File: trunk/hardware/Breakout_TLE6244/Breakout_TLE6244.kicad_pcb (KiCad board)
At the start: 2 copper layers, 1 part

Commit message: draft #1
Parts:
- removed Test: VAL**, HiQUAD64
- added C1001: 1uF, SM0805, B.Cu at (233.0, 147.3)
- added C1002: .01uF, SM0805, B.Cu at (234.9, 147.3)
- added D1001: LED-red, LED-0805_A, F.Cu at (207.6, 122.6)
- added D1002: LED-red, LED-0805_A, F.Cu at (207.6, 128.9)
- added D1003: LED-red, LED-0805_A, F.Cu at (207.6, 134.0)
- added D1004: LED-red, LED-0805_A, F.Cu at (207.6, 139.1)
- added D1005: LED-red, LED-0805_A, F.Cu at (207.6, 144.1)
- added D1006: LED-red, LED-0805_A, F.Cu at (207.6, 149.2)
- added D1007: LED-red, LED-0805_A, F.Cu at (207.6, 154.3)
- added D1008: LED-red, LED-0805_A, F.Cu at (207.6, 159.4)
- added D1009: DIODE, SOD-123, F.Cu at (203.8, 122.6)
- added D1010: DIODE, SOD-123, F.Cu at (203.8, 128.9)
- added D1011: DIODE, SOD-123, F.Cu at (203.2, 134.0)
- added D1012: DIODE, SOD-123, F.Cu at (203.2, 139.1)
- added D1013: DIODE, SOD-123, F.Cu at (203.2, 144.1)
- added D1014: DIODE, SOD-123, F.Cu at (203.2, 149.2)
- added D1015: DIODE, SOD-123, F.Cu at (203.2, 154.3)
- added D1016: DIODE, SOD-123, F.Cu at (203.2, 159.4)
- added D1017: DIODE, SOD-123, F.Cu at (215.9, 166.4)
- added D1018: LED-red, LED-0805_A, F.Cu at (211.5, 166.4)
- added D1019: DIODE, SOD-123, F.Cu at (236.2, 166.4)
- added D1020: LED-red, LED-0805_A, F.Cu at (240.7, 166.4)
- added D1021: DIODE, SOD-123, F.Cu at (249.6, 122.6)
- added D1022: DIODE, SOD-123, F.Cu at (249.6, 128.9)
- added D1023: DIODE, SOD-123, F.Cu at (249.6, 134.0)
- added D1024: DIODE, SOD-123, F.Cu at (249.6, 139.1)
- added D1025: DIODE, SOD-123, F.Cu at (249.6, 144.1)
- added D1026: DIODE, SOD-123, F.Cu at (249.6, 149.2)
- added D1027: DIODE, SOD-123, F.Cu at (249.6, 154.3)
- added D1028: DIODE, SOD-123, F.Cu at (249.6, 159.4)
- added D1029: LED-red, LED-0805_A, F.Cu at (245.1, 122.6)
- added D1030: LED-red, LED-0805_A, F.Cu at (245.1, 128.9)
- added D1031: LED-red, LED-0805_A, F.Cu at (245.1, 134.0)
- added D1032: LED-red, LED-0805_A, F.Cu at (245.1, 139.1)
- added D1033: LED-red, LED-0805_A, F.Cu at (245.1, 144.1)
- added D1034: LED-red, LED-0805_A, F.Cu at (245.1, 149.2)
- added D1035: LED-red, LED-0805_A, F.Cu at (245.1, 154.3)
- added D1036: LED-red, LED-0805_A, F.Cu at (245.1, 159.4)
- added K1001: CONN_3, bornier3, F.Cu at (196.8, 125.1)
- added K1002: CONN_3, bornier3, F.Cu at (196.8, 140.3)
- added K1003: CONN_3, bornier3, F.Cu at (196.8, 155.6)
- added K1004: CONN_3, bornier3, F.Cu at (226.1, 168.3)
- added K1005: CONN_3, bornier3, F.Cu at (255.9, 125.1)
- added K1006: CONN_3, bornier3, F.Cu at (255.9, 140.3)
- added K1007: CONN_3, bornier3, F.Cu at (255.9, 155.6)
- added P1001: CONN_10, SIL-10, F.Cu at (205.7, 170.8)
- added P1002: CONN_10, SIL-10, F.Cu at (246.4, 170.8)
- added P1003: CONN_8, SIL-8, F.Cu at (226.1, 127.6)
- added R1001: 1K, SM0805, F.Cu at (211.5, 122.6)
- added R1002: 1K, SM0805, F.Cu at (211.5, 128.9)
- added R1003: 1K, SM0805, F.Cu at (211.5, 134.0)
- added R1004: 1K, SM0805, F.Cu at (211.5, 139.1)
- added R1005: 1K, SM0805, F.Cu at (211.5, 144.1)
- added R1006: 1K, SM0805, F.Cu at (211.5, 149.2)
- added R1007: 1K, SM0805, F.Cu at (211.5, 154.3)
- added R1008: 1K, SM0805, F.Cu at (211.5, 159.4)
- added R1009: 1K, SM0805, F.Cu at (207.6, 166.4)
- added R1010: 1K, SM0805, F.Cu at (244.5, 166.4)
- added R1011: 1K, SM0805, F.Cu at (241.3, 122.6)
- added R1012: 1K, SM0805, F.Cu at (241.3, 128.9)
- added R1013: 1K, SM0805, F.Cu at (241.3, 134.0)
- added R1014: 1K, SM0805, F.Cu at (241.3, 139.1)
- added R1015: 1K, SM0805, F.Cu at (241.3, 144.1)
- added R1016: 1K, SM0805, F.Cu at (241.3, 149.2)
- added R1017: 1K, SM0805, F.Cu at (241.3, 154.3)
- added R1018: 1K, SM0805, F.Cu at (241.3, 159.4)
- added U1001: TLE6244, HiQUAD64, F.Cu at (226.1, 148.6)
- added W1001: TEST, SM0805_jumper, F.Cu at (229.2, 160.7)
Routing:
- added copper zone on PWR, net /DD_HIP9011/5V
- added copper zone on B.Cu, net GND
- added copper zone on F.Cu, net GND
- added copper zone on GND, net GND
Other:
- copper layers 2 -> 4
- net class 1A external added: clearance 0.2159, trace_width 0.3048, via_dia 0.6858, via_drill 0.3302
- net class 2.5A external added: clearance 0.2159, trace_width 1.0668, via_dia 0.6858, via_drill 0.3302
- net class 3.5A external added: clearance 0.2159, trace_width 1.651, via_dia 1.0922, via_drill 0.6858
- net class 5A external added: clearance 0.2159, trace_width 2.7178, via_dia 1.54178, via_drill 1.18618
- net class Default: clearance 0.254 -> 0.1524; trace_width 0.254 -> 0.1524; via_dia 0.889 -> 0.6858; via_drill 0.635 -> 0.3302
- net class min2_extern_.188A added: clearance 0.1524, trace_width 0.1524, via_dia 0.6858, via_drill 0.3302
- net class min_extern_.241A added: clearance 0.2159, trace_width 0.2159, via_dia 0.6858, via_drill 0.3302
- rule pad_to_mask_clearance: 0 -> 0.2
- rule trace_clearance: 0.254 -> 0.1524
- rule trace_min: 0.254 -> 0.1524
- rule via_min_drill: 0.508 -> 0.3302
- rule via_min_size: 0.889 -> 0

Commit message: fresh
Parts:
- removed C1001: 1uF, SM0805
- removed C1002: .01uF, SM0805
- removed D1017: DIODE, SOD-123
- removed D1020: LED-red, LED-0805_A
- removed P1001, P1002: CONN_10, SIL-10
- removed P1003: CONN_8, SIL-8
- added C1: 1uF, SM0805, B.Cu at (233.0, 147.3)
- added C2: .01uF, SM0805, B.Cu at (234.9, 147.3)
- added D17: DIODE, SOD-123, F.Cu at (215.9, 161.4)
- added D20: LED-red, LED-0805_A, F.Cu at (236.1, 166.2)
- added P1: CONN_4, SIL-4, F.Cu at (214.8, 138.4)
- added P2: CONN_3, SIL-3, F.Cu at (212.2, 146.0)
- added P3: CONN_2, SIL-2, F.Cu at (213.5, 148.7)
- added P4: CONN_3, SIL-3, F.Cu at (211.5, 163.8)
- added P5: CONN_5, SIL-5, F.Cu at (225.3, 133.0)
- added P6: CONN_3, SIL-3, F.Cu at (240.9, 163.8)
- added P7: CONN_2, SIL-2, F.Cu at (238.9, 145.9)
- added P8: CONN_2, SIL-2, F.Cu at (238.9, 148.7)
- moved D21 20.4 mm to (234.1, 135.9), turned to 315 degrees
- moved D9 16.8 mm to (215.0, 135.1), turned to 225 degrees
- moved K5 14.6 mm to (243.8, 133.3), turned to 0 degrees
- moved K1 14.1 mm to (208.3, 133.3), turned to 0 degrees
- moved R11 11.1 mm to (235.1, 131.7), turned to 90 degrees
- moved R1 10.4 mm to (216.9, 131.4), turned to 90 degrees
- moved D1 10.3 mm to (213.2, 131.2), turned to 0 degrees
- moved D29 9.76 mm to (239.0, 130.2), turned to 180 degrees
- moved R5 9.44 mm to (202.6, 147.3), turned to 180 degrees
- moved K7 9.38 mm to (247.7, 160.0)
- moved K6 9.38 mm to (247.7, 144.8)
- moved R6 9.25 mm to (202.8, 152.5), turned to 180 degrees
- moved R3 9.12 mm to (202.7, 136.5), turned to 180 degrees
- moved R16 8.92 mm to (249.7, 152.3), turned to 0 degrees
- moved R7 8.89 mm to (203.2, 157.6), turned to 180 degrees
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- renumbered D1001 to D1, D1010 to D10, D1011 to D11, D1012 to D12, D1013 to D13, D1014 to D14, D1015 to D15, D1016 to D16, D1018 to D18, D1019 to D19, D1002 to D2, D1021 to D21, D1022 to D22, D1023 to D23, D1024 to D24, D1025 to D25, D1026 to D26, D1027 to D27, D1028 to D28, D1029 to D29, D1003 to D3, D1030 to D30, D1031 to D31, D1032 to D32, D1033 to D33, D1034 to D34, D1035 to D35, D1036 to D36, D1004 to D4, D1005 to D5, D1006 to D6, D1007 to D7, D1008 to D8, D1009 to D9, K1001 to K1, K1002 to K2, K1003 to K3, K1004 to K4, K1005 to K5, K1006 to K6, K1007 to K7, R1001 to R1, R1010 to R10, R1011 to R11, R1012 to R12, R1013 to R13, R1014 to R14, R1015 to R15, R1016 to R16, R1017 to R17, R1018 to R18, R1002 to R2, R1003 to R3, R1004 to R4, R1005 to R5, R1006 to R6, R1007 to R7, R1008 to R8, R1009 to R9, U1001 to U1, W1001 to W1
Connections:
- D1 pad 1: N-0000033 -> /5v
- D1 pad 2: N-0000032 -> N-0000030
- D10 pad 1: N-0000043 -> N-0000044
- D11 pad 1: N-0000044 -> N-0000040
- D12 pad 1: N-0000079 -> N-0000076
- D13 pad 1: N-0000073 -> N-0000075
- D14 pad 1: N-0000076 -> N-0000073
- D15 pad 1: N-0000074 -> N-0000072
- D16 pad 1: N-0000087 -> N-0000083
- D18 pad 1: N-0000036 -> /5v
- D18 pad 2: N-0000035 -> N-0000034
- D19 pad 1: N-0000072 -> N-0000068
- D2 pad 1: N-0000048 -> /5v
- D21 pad 1: N-0000030 -> N-0000028
- D22 pad 1: N-0000046 -> N-0000041
- D23 pad 1: N-0000081 -> N-0000080
- D24 pad 1: N-0000083 -> N-0000078
- D25 pad 1: N-0000071 -> N-0000065
- D26 pad 1: N-0000069 -> N-0000063
- D27 pad 1: N-0000064 -> N-0000059
- D28 pad 1: N-0000065 -> N-0000060
- D29 pad 1: N-0000031 -> /5v
- D29 pad 2: N-0000030 -> N-0000029
- D3 pad 1: N-0000045 -> /5v
- D3 pad 2: N-0000044 -> N-0000039
- D30 pad 1: N-0000047 -> /5v
- D30 pad 2: N-0000046 -> N-0000042
- D31 pad 1: N-0000086 -> /5v
- D32 pad 1: N-0000084 -> /5v
- D32 pad 2: N-0000083 -> N-0000079
- D33 pad 1: N-0000082 -> /5v
- D33 pad 2: N-0000071 -> N-0000066
- D34 pad 1: N-0000070 -> /5v
- D34 pad 2: N-0000069 -> N-0000064
- D35 pad 1: N-0000068 -> /5v
- D35 pad 2: N-0000064 -> N-0000062
- D36 pad 1: N-0000066 -> /5v
- D36 pad 2: N-0000065 -> N-0000061
- D4 pad 1: N-0000080 -> /5v
- D4 pad 2: N-0000079 -> N-0000077
- D5 pad 1: N-0000078 -> /5v
- D5 pad 2: N-0000073 -> N-0000070
- D6 pad 1: N-0000077 -> /5v
- D6 pad 2: N-0000076 -> N-0000074
- D7 pad 1: N-0000075 -> /5v
- D7 pad 2: N-0000074 -> N-0000071
- D8 pad 1: N-0000088 -> /5v
- D8 pad 2: N-0000087 -> N-0000084
- D9 pad 1: N-0000032 -> N-0000026
- K4 pad 2: /5v -> /Ubatt
- K5 pad 2: /Ubatt -> /5v
- R1 pad 1: N-0000033 -> N-0000026
- R1 pad 2: /5v -> N-0000030
- R10 pad 1: N-0000067 -> N-0000068
- R10 pad 2: /5v -> N-0000069
- R11 pad 1: N-0000031 -> N-0000028
- R11 pad 2: /5v -> N-0000029
- R12 pad 1: N-0000047 -> N-0000041
- R12 pad 2: /5v -> N-0000042
- R13 pad 1: N-0000086 -> N-0000080
- R13 pad 2: /5v -> N-0000081
- R14 pad 1: N-0000084 -> N-0000078
- R14 pad 2: /5v -> N-0000079
- R15 pad 1: N-0000082 -> N-0000065
- R15 pad 2: /5v -> N-0000066
- R16 pad 1: N-0000070 -> N-0000063
- R16 pad 2: /5v -> N-0000064
- R17 pad 1: N-0000068 -> N-0000059
- R17 pad 2: /5v -> N-0000062
- R18 pad 1: N-0000066 -> N-0000060
- R18 pad 2: /5v -> N-0000061
- R2 pad 1: N-0000048 -> N-0000044
- R2 pad 2: /5v -> N-0000043
- R3 pad 1: N-0000045 -> N-0000040
- R3 pad 2: /5v -> N-0000039
- R4 pad 1: N-0000080 -> N-0000076
- R4 pad 2: /5v -> N-0000077
- R5 pad 1: N-0000078 -> N-0000075
- R5 pad 2: /5v -> N-0000070
- R6 pad 1: N-0000077 -> N-0000073
- R6 pad 2: /5v -> N-0000074
- R7 pad 1: N-0000075 -> N-0000072
- R7 pad 2: /5v -> N-0000071
- R8 pad 1: N-0000088 -> N-0000083
- R8 pad 2: /5v -> N-0000084
- R9 pad 1: N-0000036 -> N-0000033
- R9 pad 2: /5v -> N-0000034
- U1 pad 64: (no net) -> /in06
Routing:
- net GND: track 0.00 -> 282.4 mm, vias 0 -> 50
- net /5v: track 0.00 -> 28.2 mm, vias 0 -> 19
- net /in10: track 0.00 -> 27.8 mm
- net /out09: track 0.00 -> 24.4 mm
- net /out10: track 0.00 -> 23.6 mm
- net /out05: track 0.00 -> 22.6 mm
- net /out15: track 0.00 -> 22.5 mm
- net /out16: track 0.00 -> 22.4 mm
- net /out06: track 0.00 -> 21.9 mm
- net /out14: track 0.00 -> 20.5 mm
- net /out13: track 0.00 -> 20.3 mm
- net /out02: track 0.00 -> 18.8 mm
- net /SO: track 0.00 -> 18.8 mm
- net /out12: track 0.00 -> 18.4 mm
- net /out11: track 0.00 -> 18.3 mm
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- added copper zone on PWR, net /5v
- removed copper zone on PWR, net /DD_HIP9011/5V
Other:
- board outline added: 50.8 x 38.1 mm
- board text added: "5V"
- board text added: "GND"
- board text added: "GND RST VDDmon"
- board text added: "GNDmon GND"
- board text added: "IN01 IN05 0N11"
- board text added: "IN03 IN13"
- board text added: "IN07 IN06 0N16 IN15"
- board text added: "IN12 IN02"
- board text added: "IN14 IN04"
- board text added: "OUT07 GND OUT15"
- board text added: "OUT09 OUT05 OUT13 OUT03 OUT01 OUT11"
- board text added: "OUT10 OUT06 OUT14 OUT04 OUT02 OUT12"
- board text added: "OUT16 5V OUT08"
- board text added: "OUT18 Ubat OUT17"
- board text added: "SS SI SCK SO GND"
- board text added: "TLE6244 breakout R0.1 By DAECU for rusEFI"
- board text added: "in08 in10 in09"

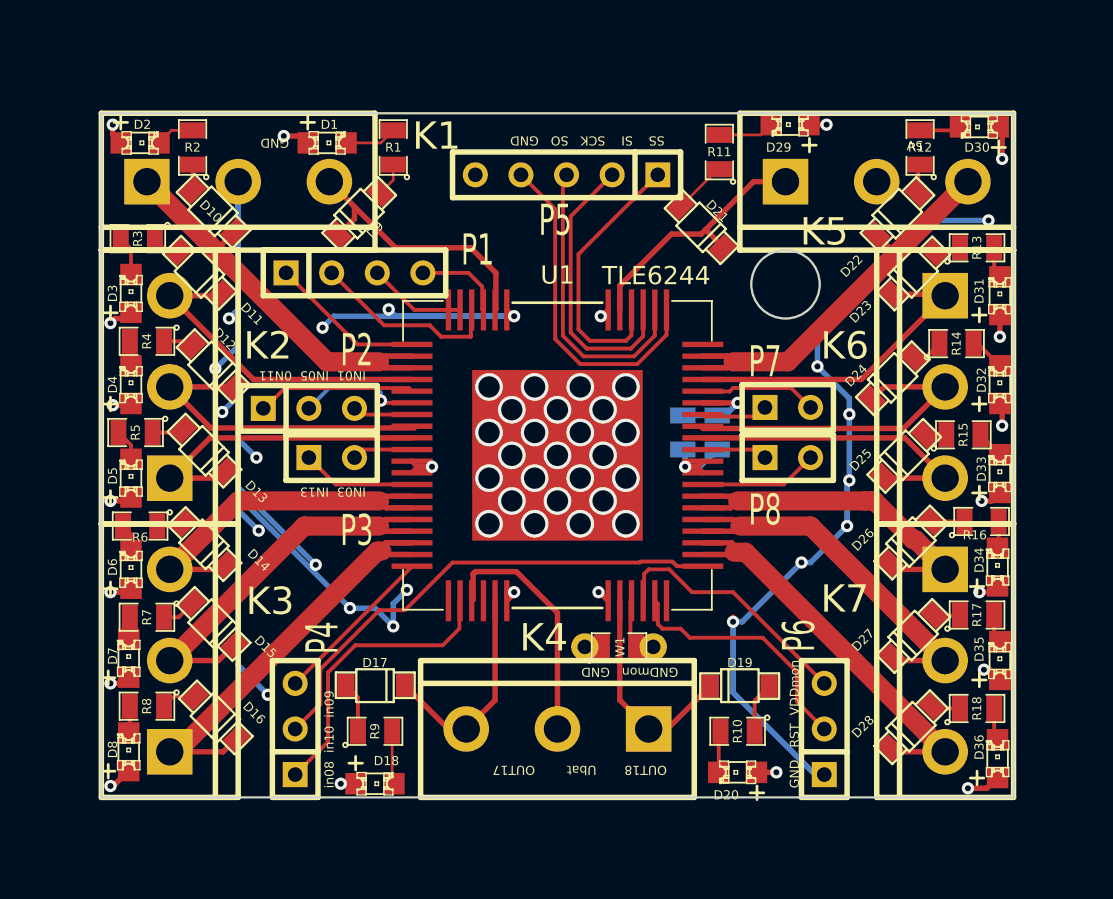
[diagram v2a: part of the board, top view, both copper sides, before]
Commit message: 
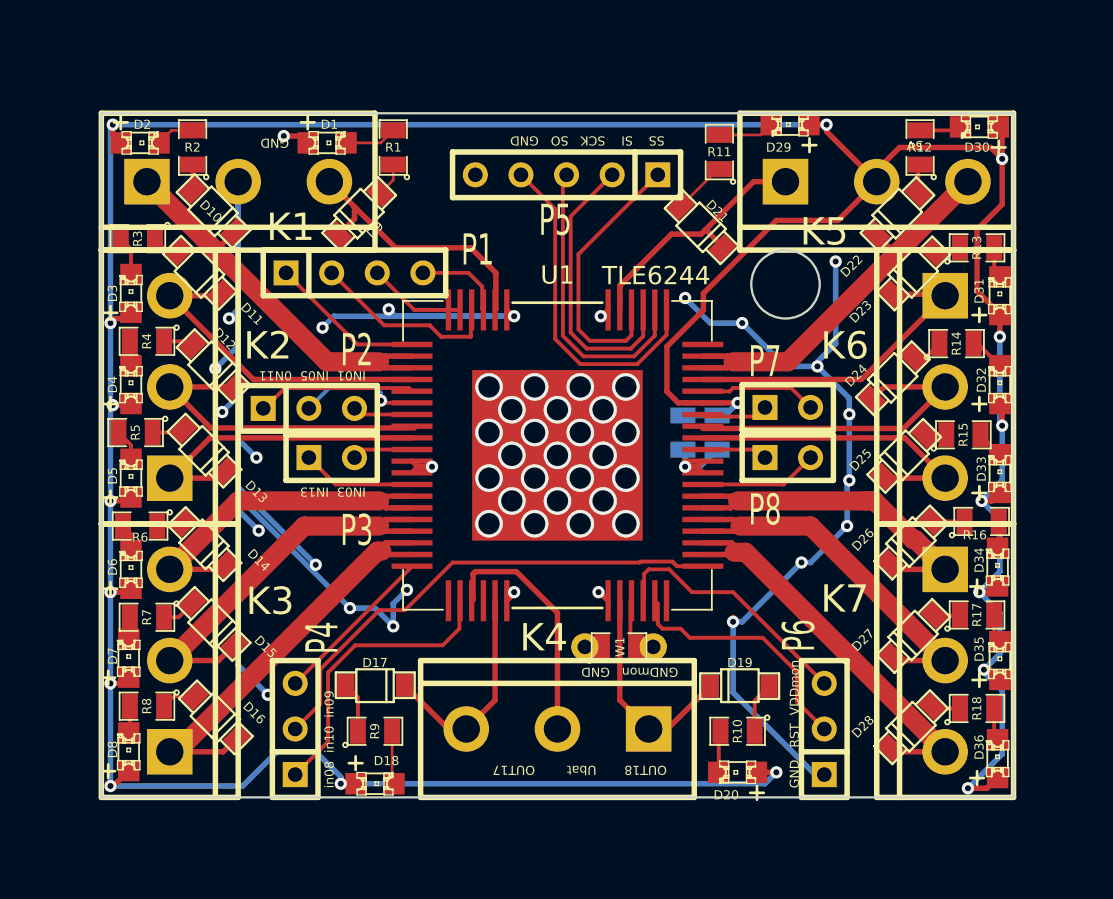
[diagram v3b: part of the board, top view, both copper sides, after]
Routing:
- net /5v: track 28.2 -> 215.8 mm
- net GND: track 282.4 -> 283.8 mm, vias 50 -> 52

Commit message: fresh version
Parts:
- moved P5 3.69 mm to (229.0, 132.7), turned to 0 degrees
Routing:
- net GND: track 283.8 -> 350.3 mm, vias 52 -> 76
- net /SO: track 18.8 -> 9.93 mm
- net /SCK: track 16.5 -> 9.34 mm
- net /SI: track 15.9 -> 10.1 mm
- net /SS: track 15.2 -> 11.8 mm
- net /out08: track 14.4 -> 16.2 mm, vias 0 -> 2
- net /in10: track 27.8 -> 28.0 mm, vias 0 -> 2
